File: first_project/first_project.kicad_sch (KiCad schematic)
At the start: 4 parts

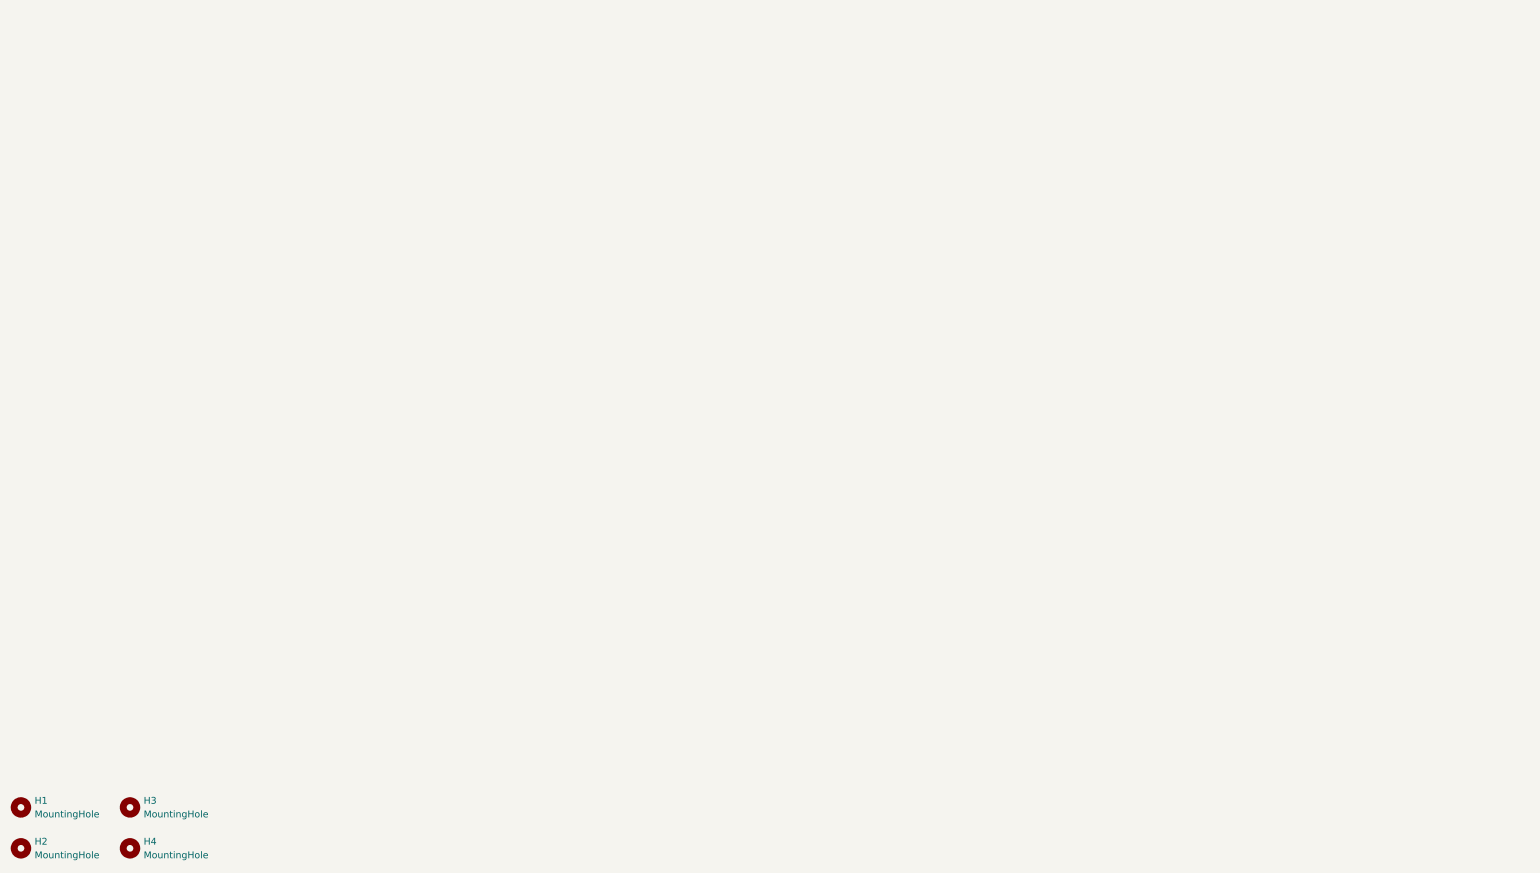
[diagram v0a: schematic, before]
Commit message: Blink speed changed and schematics
Blink speed is faster and basic schematics made by copying slide 39
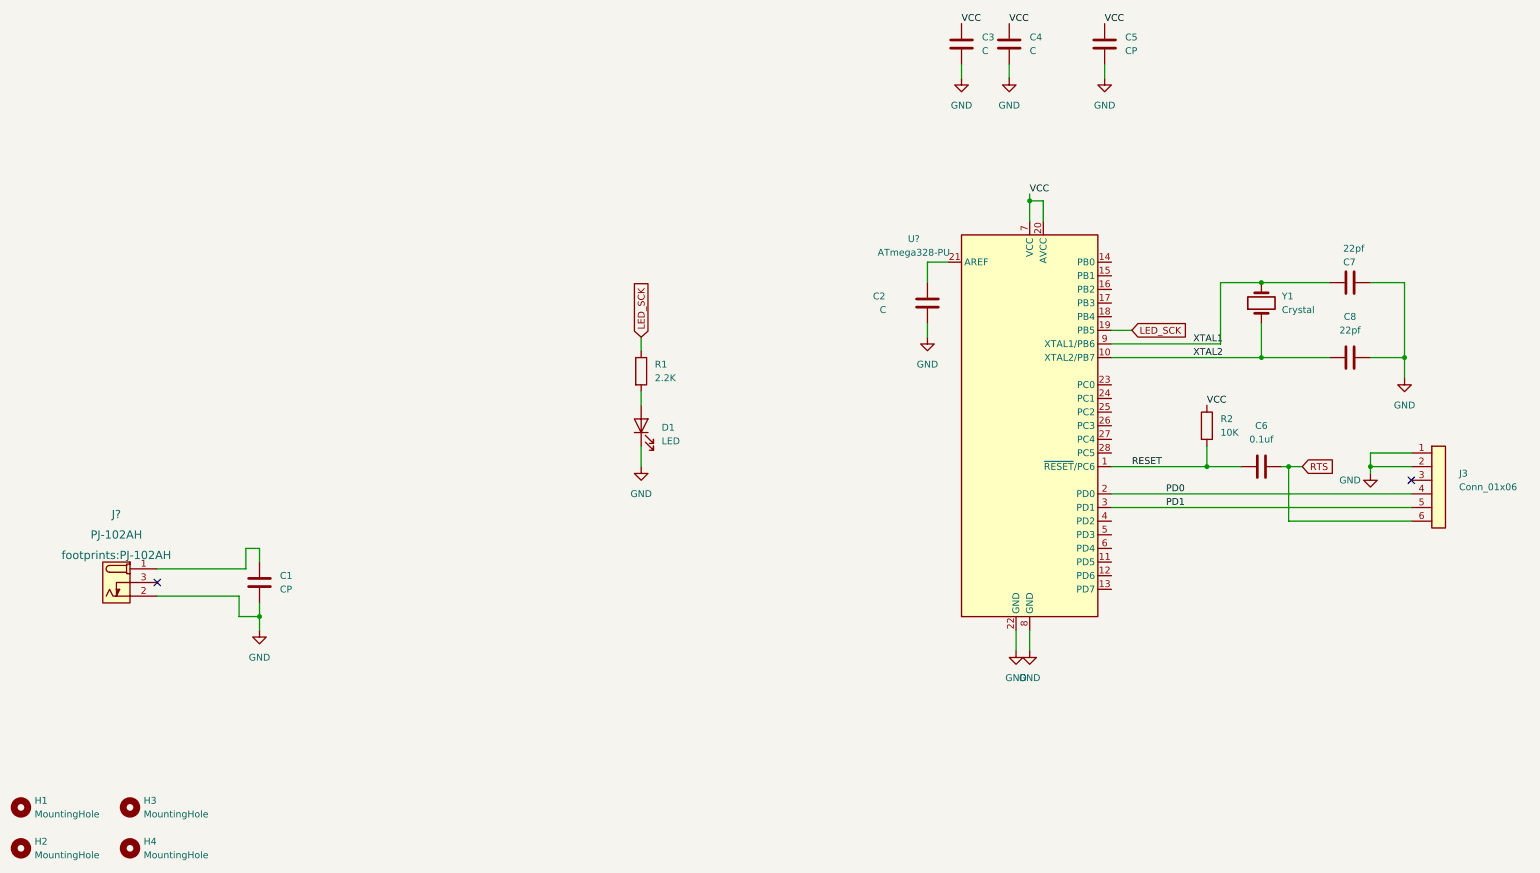
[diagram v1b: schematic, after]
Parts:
- added C1, C5: CP, footprints:C_0805_2012Metric, symbol HPS:C_0805_10uf
- added C2: C, footprints:C_0805_2012Metric, symbol HPS:C_0805_0.1uf
- added C3, C4: C, footprints:C_0805_2012Metric, symbol HPS:C_0805_1uf
- added C6: 0.1uf, footprints:C_0805_2012Metric, symbol HPS:C_0805_0.1uf
- added C7, C8: 22pf, footprints:C_0805_2012Metric, symbol HPS:C_0805_22pf
- added D1: LED, footprints:LED_0805_2012Metric, symbol HPS:LED_0805
- added J3: Conn_01x06, footprints:PinHeader_1x06_P2.54mm_Vertical, symbol HPS:Conn_01x06
- added J?: PJ-102AH, footprints:PJ-102AH, symbol HPS:PJ-102AH
- added R1: 2.2K, footprints:R_0805_2012Metric, symbol HPS:R_0805_2.2K
- added R2: 10K, footprints:R_0805_2012Metric, symbol HPS:R_0805_10K
- added U?: ATmega328-PU, footprints:DIP-28_W7.62mm, symbol HPS:ATmega328-PU
- added Y1: Crystal, footprints:Crystal_SMD_2Pin_3.2x1.5mm, symbol HPS:Crystal_32768Hz
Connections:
- new net: C1.1, J?.1 (POLE)
- new net: C2.1, U?.21 (AREF)
- new net: D1.2 (A), R1.2
- new net GND: C1.2, C2.2, C3.2, C4.2, C5.2, C7.1, C8.2, D1.1 (K), J3.1 (Pin_1), J3.2 (Pin_2), J?.2 (OUT), U?.22 (GND), U?.8 (GND)
- new net LED_SCK: R1.1, U?.19 (PB5)
- new net PD0: J3.4 (Pin_4), U?.2 (PD0)
- new net PD1: J3.5 (Pin_5), U?.3 (PD1)
- new net RESET: C6.1, R2.2, U?.1 (~{RESET}/PC6)
- new net RTS: C6.2, J3.6 (Pin_6)
- new net VCC: C3.1, C4.1, C5.1, R2.1, U?.20 (AVCC), U?.7 (VCC)
- new net XTAL1: C7.2, U?.9 (XTAL1/PB6), Y1.2
- new net XTAL2: C8.1, U?.10 (XTAL2/PB7), Y1.1
- no-connect marks 0 -> 2
